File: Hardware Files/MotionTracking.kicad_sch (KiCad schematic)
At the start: 7 parts, among them U1 LSM6DSV16XTR, U4 STM32F411RET6

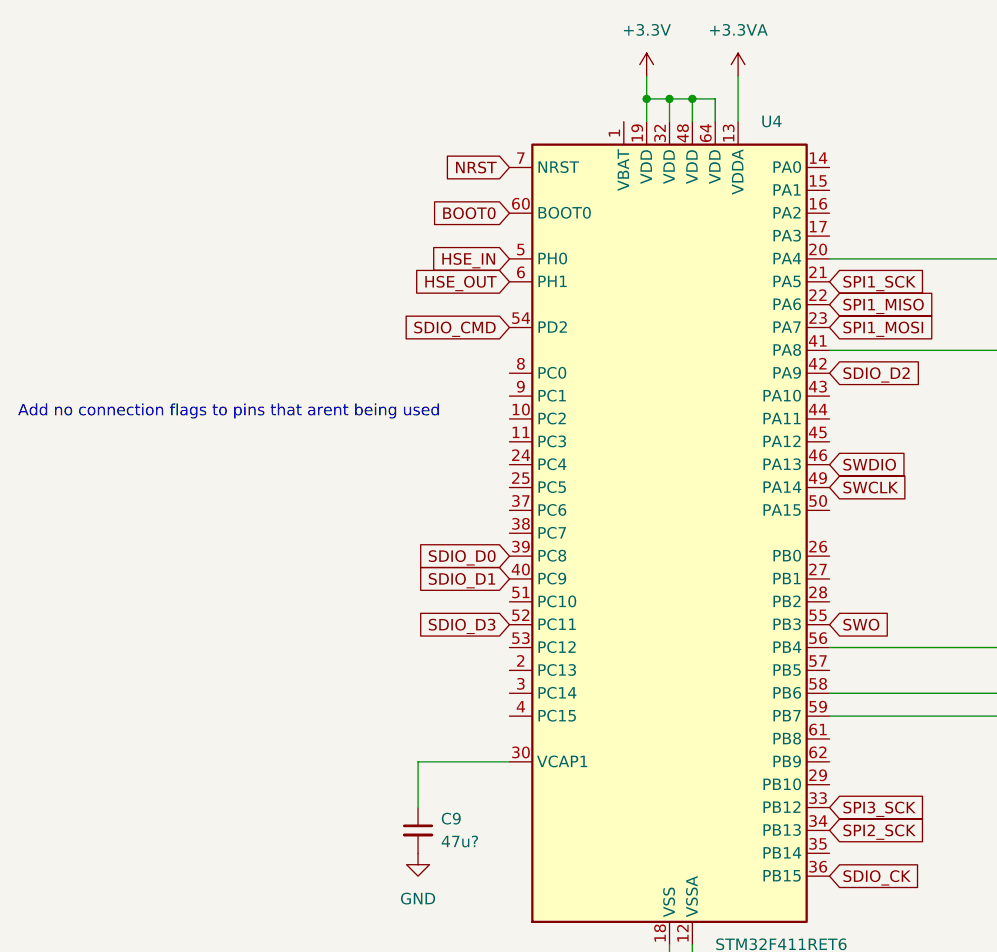
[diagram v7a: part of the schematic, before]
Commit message: Added LED indicator and NC flags
added LED for PCB debugging and LED indicator for testing the MCU functionality
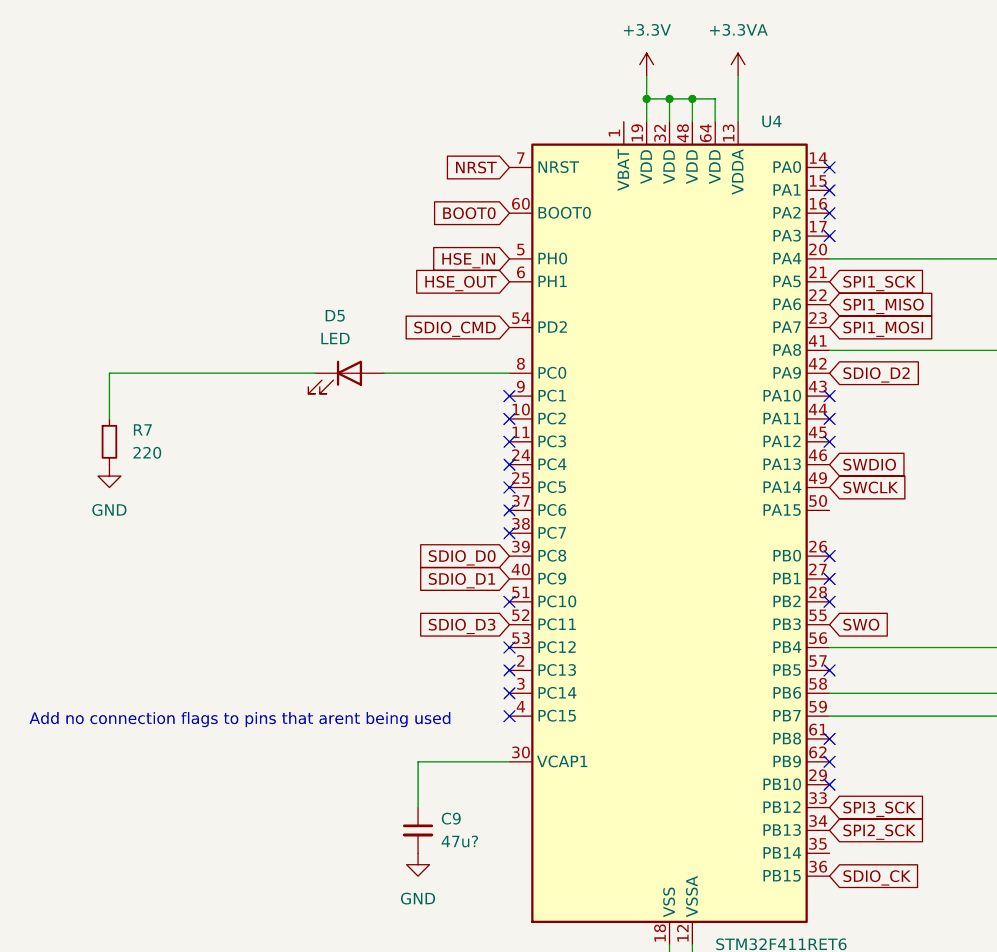
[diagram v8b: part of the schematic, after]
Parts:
- added D5: LED, symbol Device:LED
- added R7: 220, symbol Device:R_Small
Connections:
- net GND: now also R7.2
- net at U4.8 (PC0): now also D5.2 (A)
- new net: D5.1 (K), R7.1
- no-connect marks 6 -> 32
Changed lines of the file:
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@@
   (junction (at 138.43 107.95) (diameter 0) (color 0 0 0 0)
   )
+  (no_connect (at 102.87 139.7))
+  (no_connect (at 102.87 71.12))
+  (no_connect (at 102.87 116.84))
+  (no_connect (at 102.87 76.2))
+  (no_connect (at 102.87 99.06))
+  (no_connect (at 102.87 114.3))
+  (no_connect (at 102.87 137.16))
   (no_connect (at 256.54 81.28))
+  (no_connect (at 102.87 96.52))
   (no_connect (at 256.54 83.82))
+  (no_connect (at 67.31 109.22))
+  (no_connect (at 67.31 104.14))
+  (no_connect (at 102.87 134.62))
   (no_connect (at 190.5 76.2))
+  (no_connect (at 67.31 129.54))
+  (no_connect (at 102.87 78.74))
+  (no_connect (at 67.31 124.46))
+  (no_connect (at 67.31 96.52))
+  (no_connect (at 67.31 106.68))
+  (no_connect (at 67.31 111.76))
+  (no_connect (at 67.31 127))
   (no_connect (at 190.5 73.66))
+  (no_connect (at 102.87 73.66))
+  (no_connect (at 102.87 101.6))
+  (no_connect (at 67.31 132.08))
+  (no_connect (at 67.31 119.38))
   (no_connect (at 190.5 78.74))
   (no_connect (at 256.54 78.74))
+  (no_connect (at 102.87 119.38))
+  (no_connect (at 102.87 127))
+  (no_connect (at 67.31 99.06))
+  (no_connect (at 67.31 101.6))
   (wire (pts (xy 85.09 63.5) (xy 85.09 66.04))
     (stroke (width 0) (type default))
@@
     (stroke (width 0) (type default))
   )
+  (wire (pts (xy 22.86 93.98) (xy 22.86 99.06))
+    (stroke (width 0) (type default))
+  )
+  (wire (pts (xy 45.72 93.98) (xy 22.86 93.98))
+    (stroke (width 0) (type default))
+  )
   (wire (pts (xy 102.87 124.46) (xy 149.86 124.46))
     (stroke (width 0) (type default))
@@
     (stroke (width 0) (type default))
   )
+  (wire (pts (xy 53.34 93.98) (xy 67.31 93.98))
+    (stroke (width 0) (type default))
+  )
   (wire (pts (xy 261.62 66.04) (xy 256.54 66.04))
     (stroke (width 0) (type default))
@@
   )
   (text "Add no connection flags to pins that arent being used"
-    (at 12.7 99.06 0)
+    (at 13.97 133.35 0)
     (effects (font (size 1.27 1.27)) (justify left bottom))
   )
@@
     )
   )
+  (symbol (lib_id "Device:LED") (at 49.53 93.98 0) (unit 1)
+    (in_bom yes) (on_board yes) (dnp no) (fields_autoplaced)
+    (property "Reference" "D5" (at 47.9425 87.63 0)
+      (effects (font (size 1.27 1.27)))
+    )
+    (property "Value" "LED" (at 47.9425 90.17 0)
+      (effects (font (size 1.27 1.27)))
+    )
+    (property "Footprint" "" (at 49.53 93.98 0)
+      (effects (font (size 1.27 1.27)) hide)
+    )
+    (property "Datasheet" "~" (at 49.53 93.98 0)
+      (effects (font (size 1.27 1.27)) hide)
+    )
+    (pin "2")
+    (pin "1")
+    (instances
+      (project "MotionTracking"
+        (path "/111120b9-36de-4e64-8ed5-7419f276010e"
+          (reference "D5") (unit 1)
+        )
+      )
+    )
+  )
   (symbol (lib_id "imu:LSM6DSV16XTR") (at 256.54 86.36 180) (unit 1)
     (in_bom yes) (on_board yes) (dnp no) (fields_autoplaced)
@@
     )
   )
+  (symbol (lib_id "Device:R_Small") (at 22.86 101.6 0) (unit 1)
+    (in_bom yes) (on_board yes) (dnp no) (fields_autoplaced)
+    (property "Reference" "R7" (at 25.4 100.33 0)
+      (effects (font (size 1.27 1.27)) (justify left))
+    )
+    (property "Value" "220" (at 25.4 102.87 0)
+      (effects (font (size 1.27 1.27)) (justify left))
+    )
+    (property "Footprint" "" (at 22.86 101.6 0)
+      (effects (font (size 1.27 1.27)) hide)
+    )
+    (property "Datasheet" "~" (at 22.86 101.6 0)
+      (effects (font (size 1.27 1.27)) hide)
+    )
+    (pin "1")
+    (pin "2")
+    (instances
+      (project "MotionTracking"
+        (path "/111120b9-36de-4e64-8ed5-7419f276010e"
+          (reference "R7") (unit 1)
+        )
+      )
+    )
+  )
   (symbol (lib_id "power:+3.3VA") (at 92.71 60.96 0) (unit 1)
     (in_bom yes) (on_board yes) (dnp no)
@@
         )
       )
+    )
+  )
+  (symbol (lib_id "power:GND") (at 22.86 104.14 0) (unit 1)
+    (in_bom yes) (on_board yes) (dnp no) (fields_autoplaced)
+    (property "Reference" "#PWR024" (at 22.86 110.49 0)
+      (effects (font (size 1.27 1.27)) hide)
+    )
+    (property "Value" "GND" (at 22.86 109.22 0)
+      (effects (font (size 1.27 1.27)))
+    )
+    (property "Footprint" "" (at 22.86 104.14 0)
+      (effects (font (size 1.27 1.27)) hide)
+    )
+    (property "Datasheet" "" (at 22.86 104.14 0)
+      (effects (font (size 1.27 1.27)) hide)
+    )
+    (pin "1")
+    (instances
+      (project "MotionTracking"
+        (path "/111120b9-36de-4e64-8ed5-7419f276010e"
+          (reference "#PWR024") (unit 1)
+        )
+      )
